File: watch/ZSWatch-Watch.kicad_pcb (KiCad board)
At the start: 4 copper layers, 40.5 x 37.5 mm, 71 parts, among them IC401 nPM1300-QEXX, IC501 APDS-9306-065, IC502 BMI270, IC503 LIS2MDLTR, IC504 BMP581, IC505 DRV2603RUNT, IC506 PCA9306JK, IC507 RV-8263-C8, IC601 FAN5622SX, IC602 USBLC6-2P6, IC603 MX25U51245GZ4I00, IC604 NTS0104GU12, J1 53261-0271, M601 NORA-B106, X509 Motor, X603 Device, X608 Display, X701 MB1, X702 MB2

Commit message: Update schematic and layout with KiCad 10
Changes to the MCU and Power sheets and the layout, saved with KiCad 10
(adds the new KiCad 10 project settings).

Co-Authored-By: Claude Opus 5.5 <noreply@anthropic.com>
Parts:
- TP4, TP5, TP6, TP7, TP8: footprint TestPoint:TestPoint_Pad_D1.0mm -> Testpoints_Kampi:TestPoint_Pad_D1.0mm

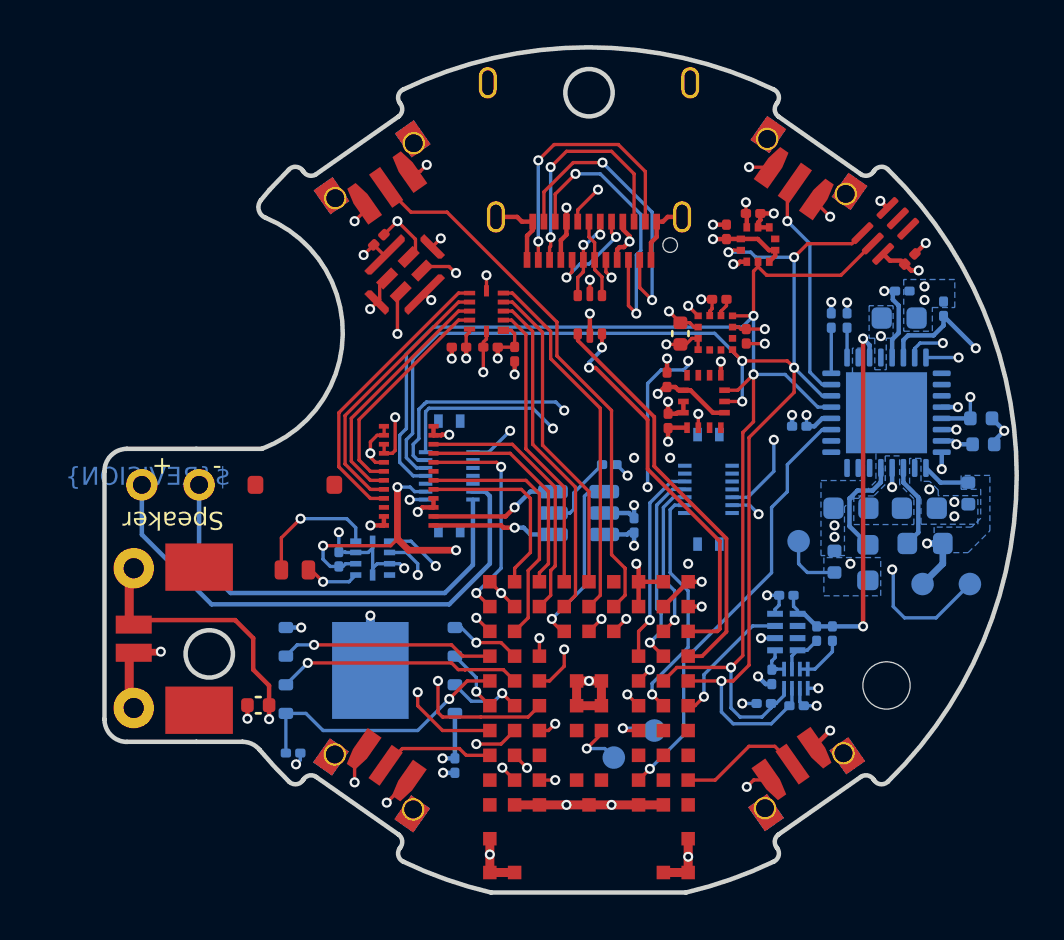
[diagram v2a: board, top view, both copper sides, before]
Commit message: Fix DRC errors and remove the Power - Topology sheet
Fixes the annular width of the mounting holes of S501 to S504 and the
courtyard overlaps of J1 with C403 and X509. The removed sheet also fixes the
duplicate page number 2.

Co-Authored-By: Claude Opus 5.5 <noreply@anthropic.com>
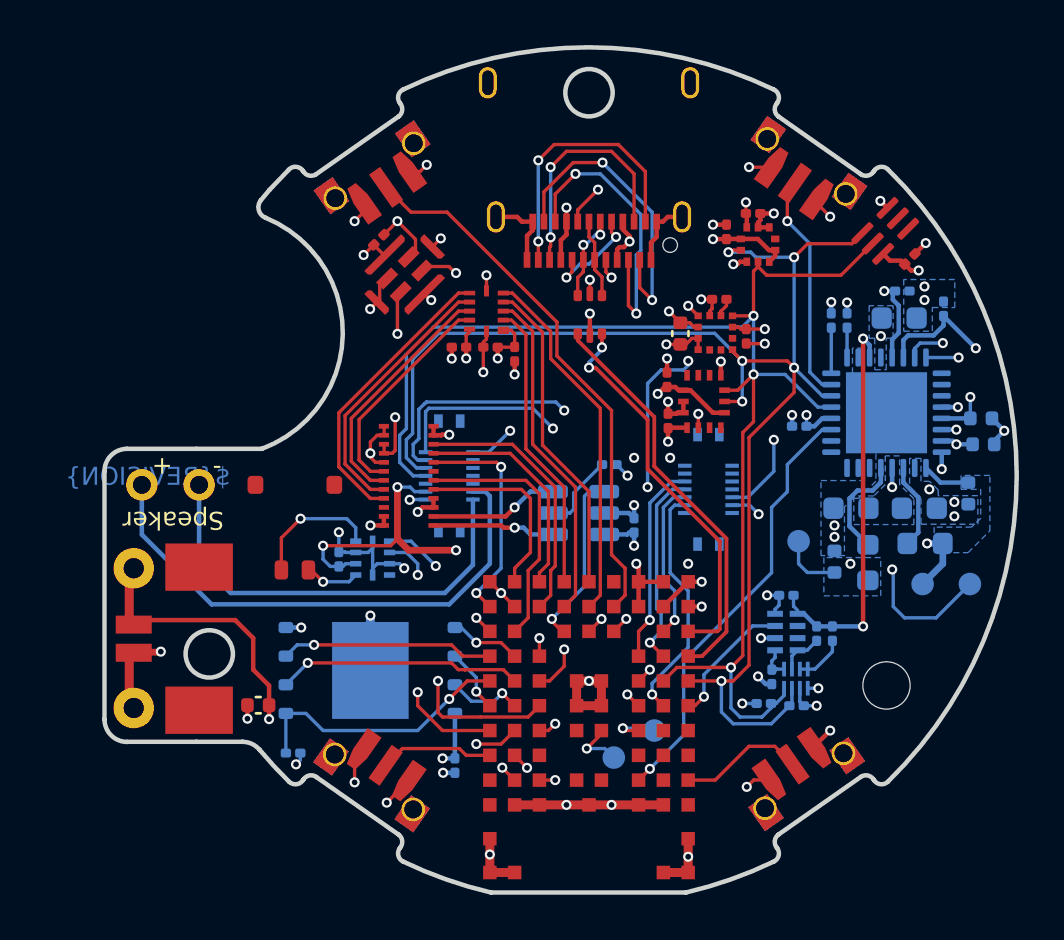
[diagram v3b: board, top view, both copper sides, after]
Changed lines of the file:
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@@
 		(sheetname "/Project Architecture/Peripherals/")
 		(sheetfile "Peripherals.kicad_sch")
-		(units
-			(unit
-				(name "A")
-				(pins "1" "2")
-			)
-		)
 		(attr through_hole)
 		(duplicate_pad_numbers_are_jumpers no)
@@
 		(pad "MH" thru_hole circle
 			(at -2.125 -0.087 145)
-			(size 1 1)
+			(size 1.05 1.05)
 			(drill 0.8)
 			(layers "*.Cu" "*.Mask")
@@
 		(pad "MH" thru_hole circle
 			(at 2.125 -0.087 145)
-			(size 1 1)
+			(size 1.05 1.05)
 			(drill 0.8)
 			(layers "*.Cu" "*.Mask")
@@
 		(sheetname "/Project Architecture/Peripherals/")
 		(sheetfile "Peripherals.kicad_sch")
-		(units
-			(unit
-				(name "A")
-				(pins "1" "2")
-			)
-		)
 		(attr through_hole)
 		(duplicate_pad_numbers_are_jumpers no)
@@
 		(pad "MH" thru_hole circle
 			(at -2.125 -0.087 325)
-			(size 1 1)
+			(size 1.05 1.05)
 			(drill 0.8)
 			(layers "*.Cu" "*.Mask")
@@
 		(pad "MH" thru_hole circle
 			(at 2.125 -0.087 325)
-			(size 1 1)
+			(size 1.05 1.05)
 			(drill 0.8)
 			(layers "*.Cu" "*.Mask")
@@
 		(sheetname "/Project Architecture/Peripherals/")
 		(sheetfile "Peripherals.kicad_sch")
-		(units
-			(unit
-				(name "A")
-				(pins "1" "2")
-			)
-		)
 		(attr through_hole)
 		(duplicate_pad_numbers_are_jumpers no)
@@
 		(pad "MH" thru_hole circle
 			(at -2.125 -0.087 35)
-			(size 1 1)
+			(size 1.05 1.05)
 			(drill 0.8)
 			(layers "*.Cu" "*.Mask")
@@
 		(pad "MH" thru_hole circle
 			(at 2.125 -0.087 35)
-			(size 1 1)
+			(size 1.05 1.05)
 			(drill 0.8)
 			(layers "*.Cu" "*.Mask")
@@
 		(sheetname "/Project Architecture/Peripherals/")
 		(sheetfile "Peripherals.kicad_sch")
-		(units
-			(unit
-				(name "A")
-				(pins "1" "2")
-			)
-		)
 		(attr through_hole)
 		(duplicate_pad_numbers_are_jumpers no)
@@
 		(pad "MH" thru_hole circle
 			(at -2.125 -0.087 215)
-			(size 1 1)
+			(size 1.05 1.05)
 			(drill 0.8)
 			(layers "*.Cu" "*.Mask")
@@
 		(pad "MH" thru_hole circle
 			(at 2.125 -0.087 215)
-			(size 1 1)
+			(size 1.05 1.05)
 			(drill 0.8)
 			(layers "*.Cu" "*.Mask")
